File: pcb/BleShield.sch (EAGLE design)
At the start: 22 parts, among them U1 ARDUINO_SHIELDNOHOLES, Y1 32.768KHz, 10 PPM

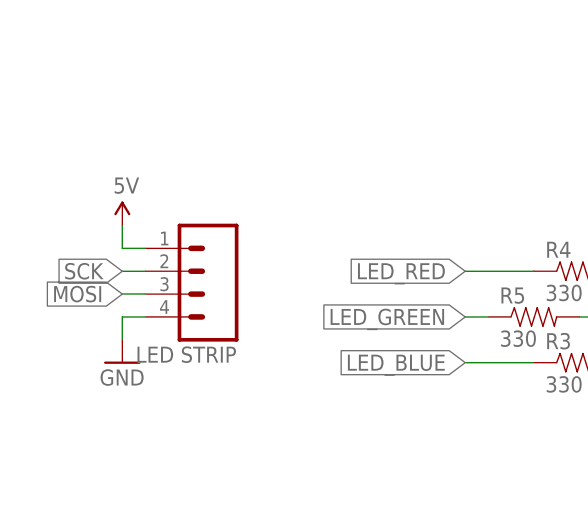
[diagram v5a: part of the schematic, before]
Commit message: fixed LED strip header, minor re-routing
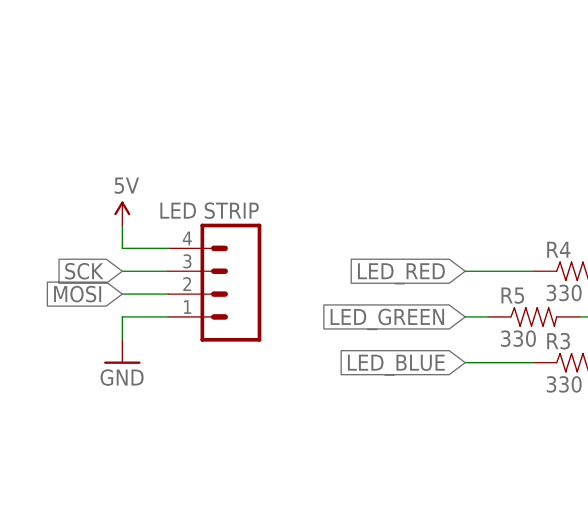
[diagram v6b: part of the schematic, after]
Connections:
- net 5V: now also LED STRIP.4; no longer LED STRIP.1
- net GND: now also LED STRIP.1; no longer LED STRIP.4
- net MOSI: now also LED STRIP.2; no longer LED STRIP.3
- net SCK: now also LED STRIP.3; no longer LED STRIP.2
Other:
- moved on the sheet: LED STRIP
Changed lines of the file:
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@@
 <instance part="GND6" gate="1" x="114.3" y="17.78"/>
 <instance part="R6" gate="G$1" x="104.14" y="83.82"/>
-<instance part="LED STRIP" gate="G$1" x="27.94" y="30.48" rot="R180"/>
+<instance part="LED STRIP" gate="G$1" x="30.48" y="27.94" rot="MR0"/>
 <instance part="GND7" gate="1" x="20.32" y="20.32"/>
 <instance part="U$2" gate="G$1" x="20.32" y="35.56"/>
@@
 </segment>
 <segment>
-<pinref part="LED STRIP" gate="G$1" pin="4"/>
-<wire x1="22.86" y1="25.4" x2="20.32" y2="25.4" width="0.1524" layer="91"/>
 <pinref part="GND7" gate="1" pin="GND"/>
 <wire x1="20.32" y1="25.4" x2="20.32" y2="22.86" width="0.1524" layer="91"/>
+<pinref part="LED STRIP" gate="G$1" pin="1"/>
+<wire x1="20.32" y1="25.4" x2="25.4" y2="25.4" width="0.1524" layer="91"/>
 </segment>
 <segment>
@@
 </segment>
 <segment>
-<pinref part="LED STRIP" gate="G$1" pin="3"/>
-<wire x1="22.86" y1="27.94" x2="20.32" y2="27.94" width="0.1524" layer="91"/>
+<pinref part="LED STRIP" gate="G$1" pin="2"/>
+<wire x1="25.4" y1="27.94" x2="20.32" y2="27.94" width="0.1524" layer="91"/>
 <label x="20.32" y="27.94" size="1.778" layer="95" rot="R180" xref="yes"/>
 </segment>
@@
 </segment>
 <segment>
-<pinref part="LED STRIP" gate="G$1" pin="2"/>
-<wire x1="22.86" y1="30.48" x2="20.32" y2="30.48" width="0.1524" layer="91"/>
+<pinref part="LED STRIP" gate="G$1" pin="3"/>
+<wire x1="25.4" y1="30.48" x2="20.32" y2="30.48" width="0.1524" layer="91"/>
 <label x="20.32" y="30.48" size="1.778" layer="95" rot="R180" xref="yes"/>
 </segment>
@@
 </segment>
 <segment>
-<pinref part="LED STRIP" gate="G$1" pin="1"/>
-<wire x1="22.86" y1="33.02" x2="20.32" y2="33.02" width="0.1524" layer="91"/>
 <pinref part="U$2" gate="G$1" pin="5V"/>
 <wire x1="20.32" y1="33.02" x2="20.32" y2="35.56" width="0.1524" layer="91"/>
-</segment>
-<segment>
+<pinref part="LED STRIP" gate="G$1" pin="4"/>
+<wire x1="20.32" y1="33.02" x2="25.4" y2="33.02" width="0.1524" layer="91"/>
+</segment>
+<segment>

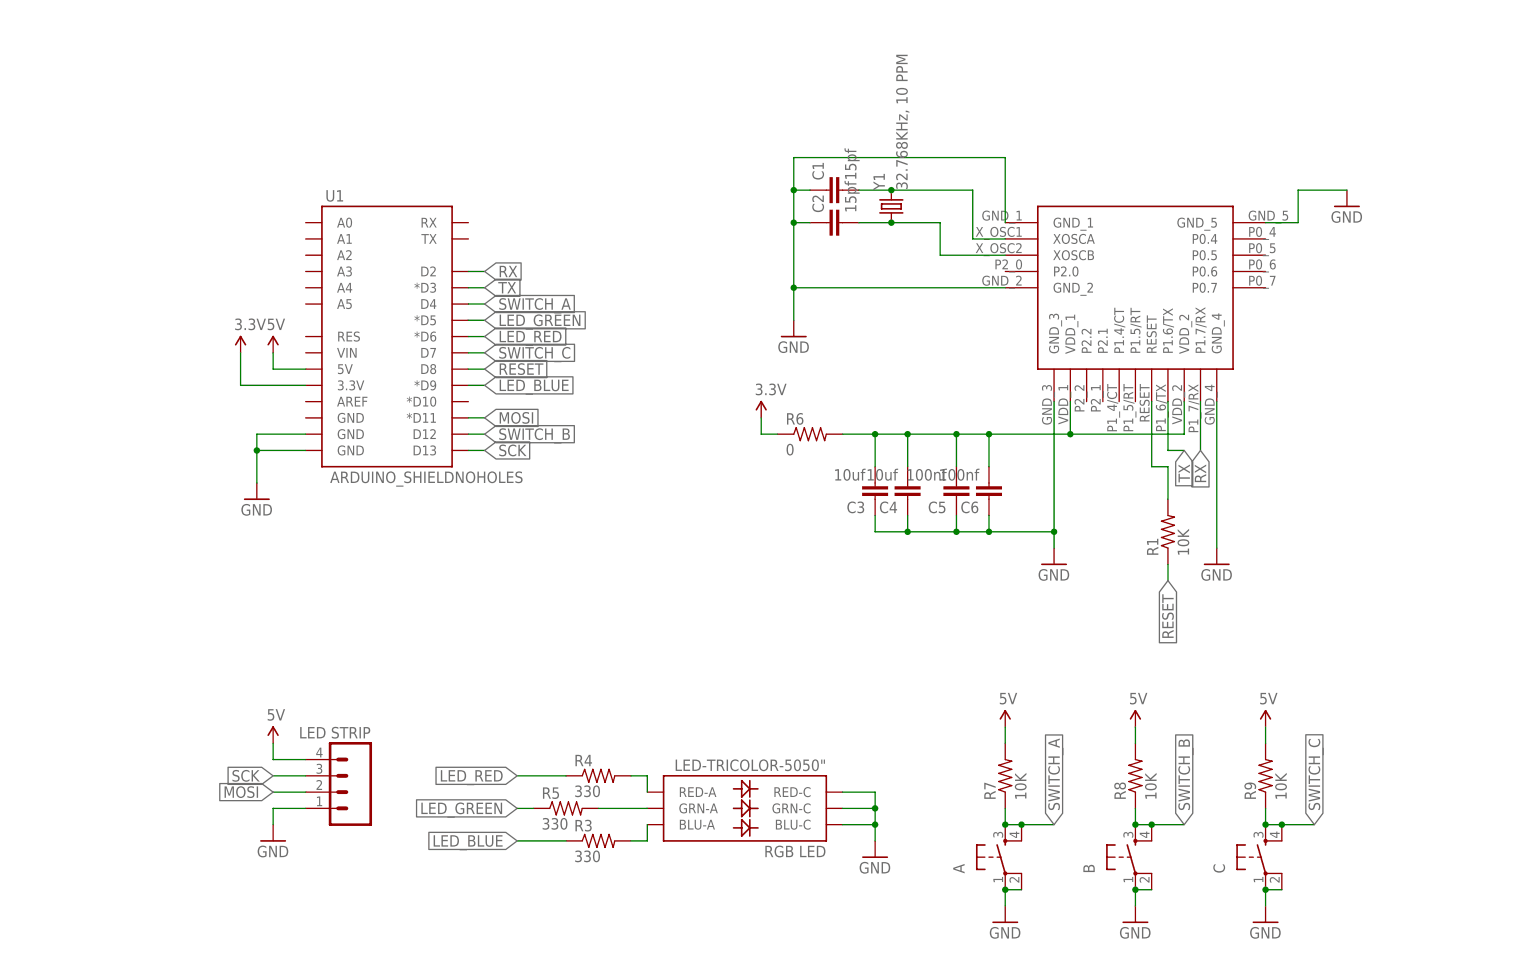
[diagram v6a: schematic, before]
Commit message: Update documentation, layout
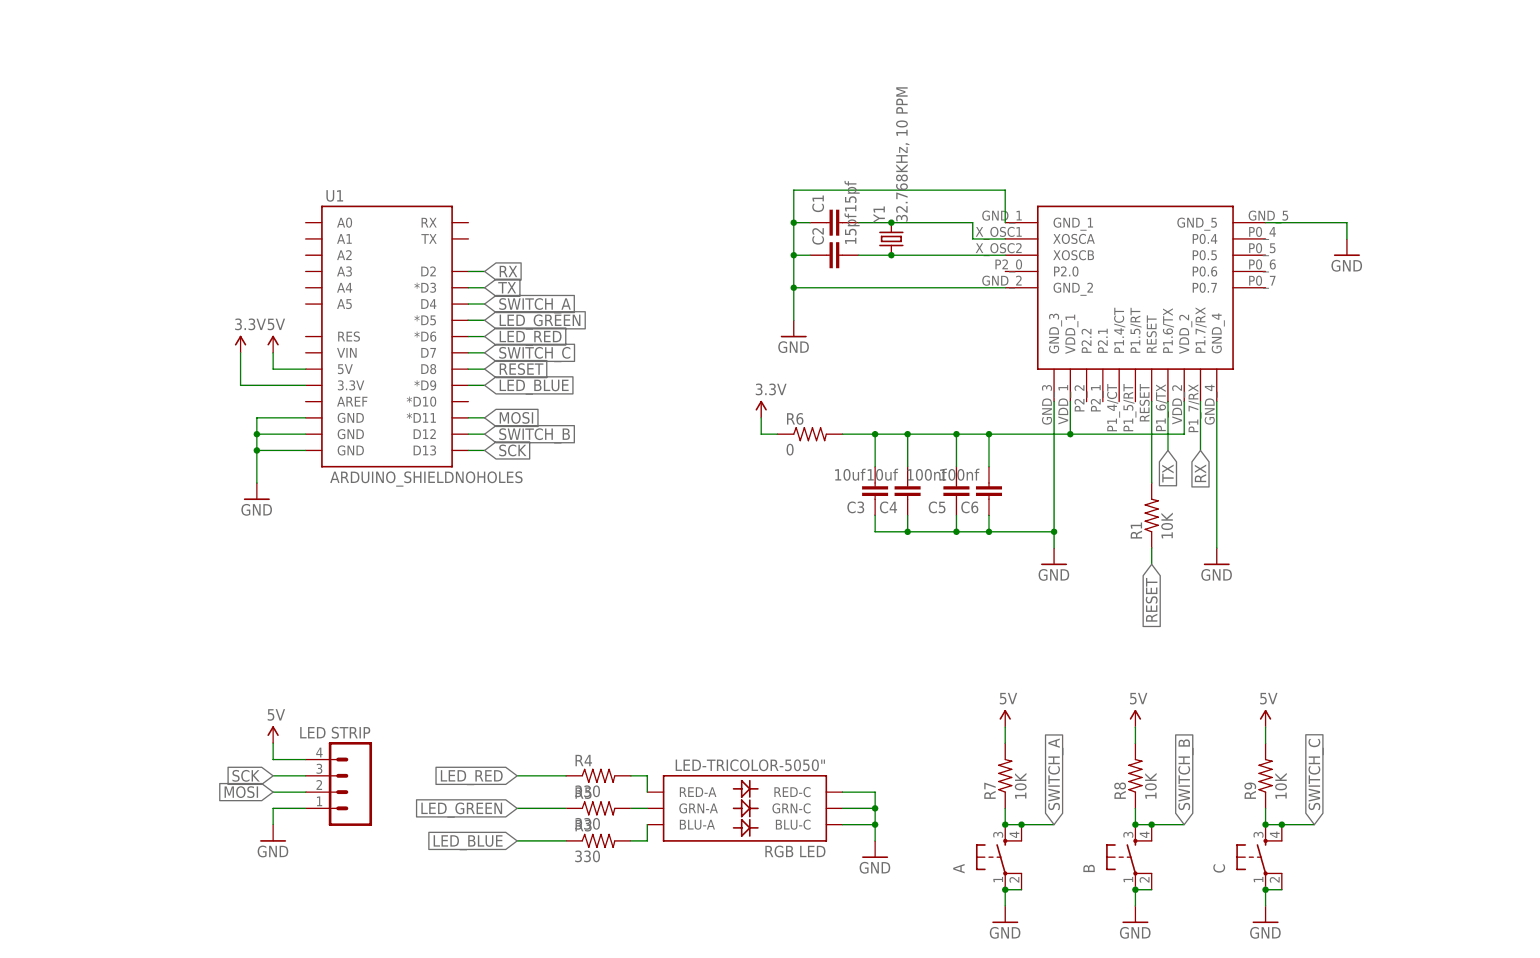
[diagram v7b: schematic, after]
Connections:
- net GND: now also U1.GND@2
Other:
- moved on the sheet: C1, C2, R1, R5, Y1
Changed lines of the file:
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@@
 <instance part="GND2" gate="1" x="142.24" y="63.5"/>
 <instance part="GND3" gate="1" x="101.6" y="99.06"/>
-<instance part="R1" gate="G$1" x="160.02" y="68.58" rot="R90"/>
-<instance part="GND4" gate="1" x="187.96" y="119.38"/>
+<instance part="R1" gate="G$1" x="157.48" y="71.12" rot="R90"/>
+<instance part="GND4" gate="1" x="187.96" y="111.76"/>
 <instance part="GND5" gate="1" x="167.64" y="63.5"/>
-<instance part="C1" gate="G$1" x="109.22" y="121.92" rot="R90"/>
-<instance part="C2" gate="G$1" x="109.22" y="116.84" rot="R90"/>
+<instance part="C1" gate="G$1" x="109.22" y="116.84" rot="R90"/>
+<instance part="C2" gate="G$1" x="109.22" y="111.76" rot="R90"/>
 <instance part="C3" gate="G$1" x="114.3" y="76.2" rot="R180"/>
 <instance part="C4" gate="G$1" x="119.38" y="76.2" rot="R180"/>
@@
 <instance part="R3" gate="G$1" x="71.12" y="20.32"/>
 <instance part="R4" gate="G$1" x="71.12" y="30.48"/>
-<instance part="R5" gate="G$1" x="66.04" y="25.4"/>
+<instance part="R5" gate="G$1" x="71.12" y="25.4"/>
 <instance part="GND6" gate="1" x="114.3" y="17.78"/>
 <instance part="R6" gate="G$1" x="104.14" y="83.82"/>
@@
 <instance part="GND10" gate="1" x="175.26" y="7.62"/>
 <instance part="RGB LED" gate="G$1" x="93.98" y="25.4" rot="R180"/>
-<instance part="Y1" gate="G$1" x="116.84" y="119.38" rot="R90"/>
+<instance part="Y1" gate="G$1" x="116.84" y="114.3" rot="R90"/>
 <instance part="A" gate="S" x="134.62" y="17.78" rot="R90"/>
 </instances>
@@
 <segment>
 <pinref part="U$1" gate="G$1" pin="P1.6/TX"/>
-<label x="162.56" y="81.28" size="1.778" layer="95" rot="R270" xref="yes"/>
-<wire x1="162.56" y1="81.28" x2="160.02" y2="81.28" width="0.1524" layer="91"/>
+<label x="160.02" y="81.28" size="1.778" layer="95" rot="R270" xref="yes"/>
 <wire x1="160.02" y1="81.28" x2="160.02" y2="88.9" width="0.1524" layer="91"/>
 </segment>
@@
 <wire x1="25.4" y1="81.28" x2="17.78" y2="81.28" width="0.1524" layer="91"/>
 <junction x="17.78" y="81.28"/>
+<pinref part="U1" gate="G$1" pin="GND@2"/>
+<wire x1="25.4" y1="86.36" x2="17.78" y2="86.36" width="0.1524" layer="91"/>
+<wire x1="17.78" y1="86.36" x2="17.78" y2="83.82" width="0.1524" layer="91"/>
+<junction x="17.78" y="83.82"/>
 </segment>
 <segment>
@@
 <wire x1="101.6" y1="106.68" x2="101.6" y2="101.6" width="0.1524" layer="91"/>
 <pinref part="U$1" gate="G$1" pin="GND_1"/>
-<wire x1="134.62" y1="116.84" x2="134.62" y2="127" width="0.1524" layer="91"/>
-<wire x1="134.62" y1="127" x2="101.6" y2="127" width="0.1524" layer="91"/>
-<wire x1="101.6" y1="127" x2="101.6" y2="121.92" width="0.1524" layer="91"/>
+<wire x1="134.62" y1="116.84" x2="134.62" y2="121.92" width="0.1524" layer="91"/>
+<wire x1="134.62" y1="121.92" x2="101.6" y2="121.92" width="0.1524" layer="91"/>
+<wire x1="101.6" y1="121.92" x2="101.6" y2="116.84" width="0.1524" layer="91"/>
 <junction x="101.6" y="106.68"/>
-<wire x1="101.6" y1="121.92" x2="101.6" y2="116.84" width="0.1524" layer="91"/>
-<wire x1="101.6" y1="116.84" x2="101.6" y2="106.68" width="0.1524" layer="91"/>
+<wire x1="101.6" y1="116.84" x2="101.6" y2="111.76" width="0.1524" layer="91"/>
+<wire x1="101.6" y1="111.76" x2="101.6" y2="106.68" width="0.1524" layer="91"/>
 <pinref part="C1" gate="G$1" pin="1"/>
-<wire x1="104.14" y1="121.92" x2="101.6" y2="121.92" width="0.1524" layer="91"/>
+<wire x1="104.14" y1="116.84" x2="101.6" y2="116.84" width="0.1524" layer="91"/>
 <pinref part="C2" gate="G$1" pin="1"/>
-<wire x1="104.14" y1="116.84" x2="101.6" y2="116.84" width="0.1524" layer="91"/>
-<junction x="101.6" y="121.92"/>
+<wire x1="104.14" y1="111.76" x2="101.6" y2="111.76" width="0.1524" layer="91"/>
 <junction x="101.6" y="116.84"/>
+<junction x="101.6" y="111.76"/>
 </segment>
 <segment>
@@
 <pinref part="U$1" gate="G$1" pin="GND_5"/>
 <pinref part="GND4" gate="1" pin="GND"/>
-<wire x1="175.26" y1="116.84" x2="180.34" y2="116.84" width="0.1524" layer="91"/>
-<wire x1="187.96" y1="121.92" x2="180.34" y2="121.92" width="0.1524" layer="91"/>
-<wire x1="180.34" y1="121.92" x2="180.34" y2="116.84" width="0.1524" layer="91"/>
+<wire x1="187.96" y1="114.3" x2="187.96" y2="116.84" width="0.1524" layer="91"/>
+<wire x1="187.96" y1="116.84" x2="175.26" y2="116.84" width="0.1524" layer="91"/>
 </segment>
 <segment>
@@
 <pinref part="U$1" gate="G$1" pin="RESET"/>
 <pinref part="R1" gate="G$1" pin="2"/>
-<wire x1="157.48" y1="88.9" x2="157.48" y2="78.74" width="0.1524" layer="91"/>
-<wire x1="157.48" y1="78.74" x2="160.02" y2="78.74" width="0.1524" layer="91"/>
-<wire x1="160.02" y1="78.74" x2="160.02" y2="73.66" width="0.1524" layer="91"/>
+<wire x1="157.48" y1="88.9" x2="157.48" y2="76.2" width="0.1524" layer="91"/>
 </segment>
 </net>
@@
 <segment>
 <pinref part="R1" gate="G$1" pin="1"/>
-<wire x1="160.02" y1="63.5" x2="160.02" y2="60.96" width="0.1524" layer="91"/>
-<label x="160.02" y="60.96" size="1.778" layer="95" rot="R270" xref="yes"/>
+<wire x1="157.48" y1="66.04" x2="157.48" y2="63.5" width="0.1524" layer="91"/>
+<label x="157.48" y="63.5" size="1.778" layer="95" rot="R270" xref="yes"/>
 </segment>
 <segment>
@@
 <segment>
 <pinref part="C1" gate="G$1" pin="2"/>
-<wire x1="111.76" y1="121.92" x2="116.84" y2="121.92" width="0.1524" layer="91"/>
-<wire x1="116.84" y1="121.92" x2="129.54" y2="121.92" width="0.1524" layer="91"/>
-<wire x1="129.54" y1="121.92" x2="129.54" y2="114.3" width="0.1524" layer="91"/>
+<wire x1="111.76" y1="116.84" x2="116.84" y2="116.84" width="0.1524" layer="91"/>
+<wire x1="116.84" y1="116.84" x2="129.54" y2="116.84" width="0.1524" layer="91"/>
+<wire x1="129.54" y1="116.84" x2="129.54" y2="114.3" width="0.1524" layer="91"/>
 <pinref part="U$1" gate="G$1" pin="XOSCA"/>
 <wire x1="129.54" y1="114.3" x2="134.62" y2="114.3" width="0.1524" layer="91"/>
 <pinref part="Y1" gate="G$1" pin="2"/>
-<junction x="116.84" y="121.92"/>
+<junction x="116.84" y="116.84"/>
 </segment>
 </net>
@@
 <segment>
 <pinref part="U$1" gate="G$1" pin="XOSCB"/>
-<wire x1="134.62" y1="111.76" x2="124.46" y2="111.76" width="0.1524" layer="91"/>
-<wire x1="124.46" y1="111.76" x2="124.46" y2="116.84" width="0.1524" layer="91"/>
-<wire x1="124.46" y1="116.84" x2="116.84" y2="116.84" width="0.1524" layer="91"/>
+<wire x1="134.62" y1="111.76" x2="116.84" y2="111.76" width="0.1524" layer="91"/>
 <pinref part="C2" gate="G$1" pin="2"/>
 <pinref part="Y1" gate="G$1" pin="1"/>
-<wire x1="116.84" y1="116.84" x2="111.76" y2="116.84" width="0.1524" layer="91"/>
-<junction x="116.84" y="116.84"/>
+<wire x1="116.84" y1="111.76" x2="111.76" y2="111.76" width="0.1524" layer="91"/>
+<junction x="116.84" y="111.76"/>
 </segment>
 </net>
@@
 <segment>
 <pinref part="R5" gate="G$1" pin="1"/>
-<wire x1="60.96" y1="25.4" x2="58.42" y2="25.4" width="0.1524" layer="91"/>
+<wire x1="66.04" y1="25.4" x2="58.42" y2="25.4" width="0.1524" layer="91"/>
 <label x="58.42" y="25.4" size="1.778" layer="95" rot="R180" xref="yes"/>
 </segment>
@@
 <pinref part="R5" gate="G$1" pin="2"/>
 <pinref part="RGB LED" gate="G$1" pin="GRN-A"/>
-<wire x1="71.12" y1="25.4" x2="78.74" y2="25.4" width="0.1524" layer="91"/>
-</segment>
-</net>
+<wire x1="76.2" y1="25.4" x2="78.74" y2="25.4" width="0.1524" layer="91"/>
+</segment>
+</net>

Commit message: Add keepaway, cutout to BLE part, knock out some to-do items.
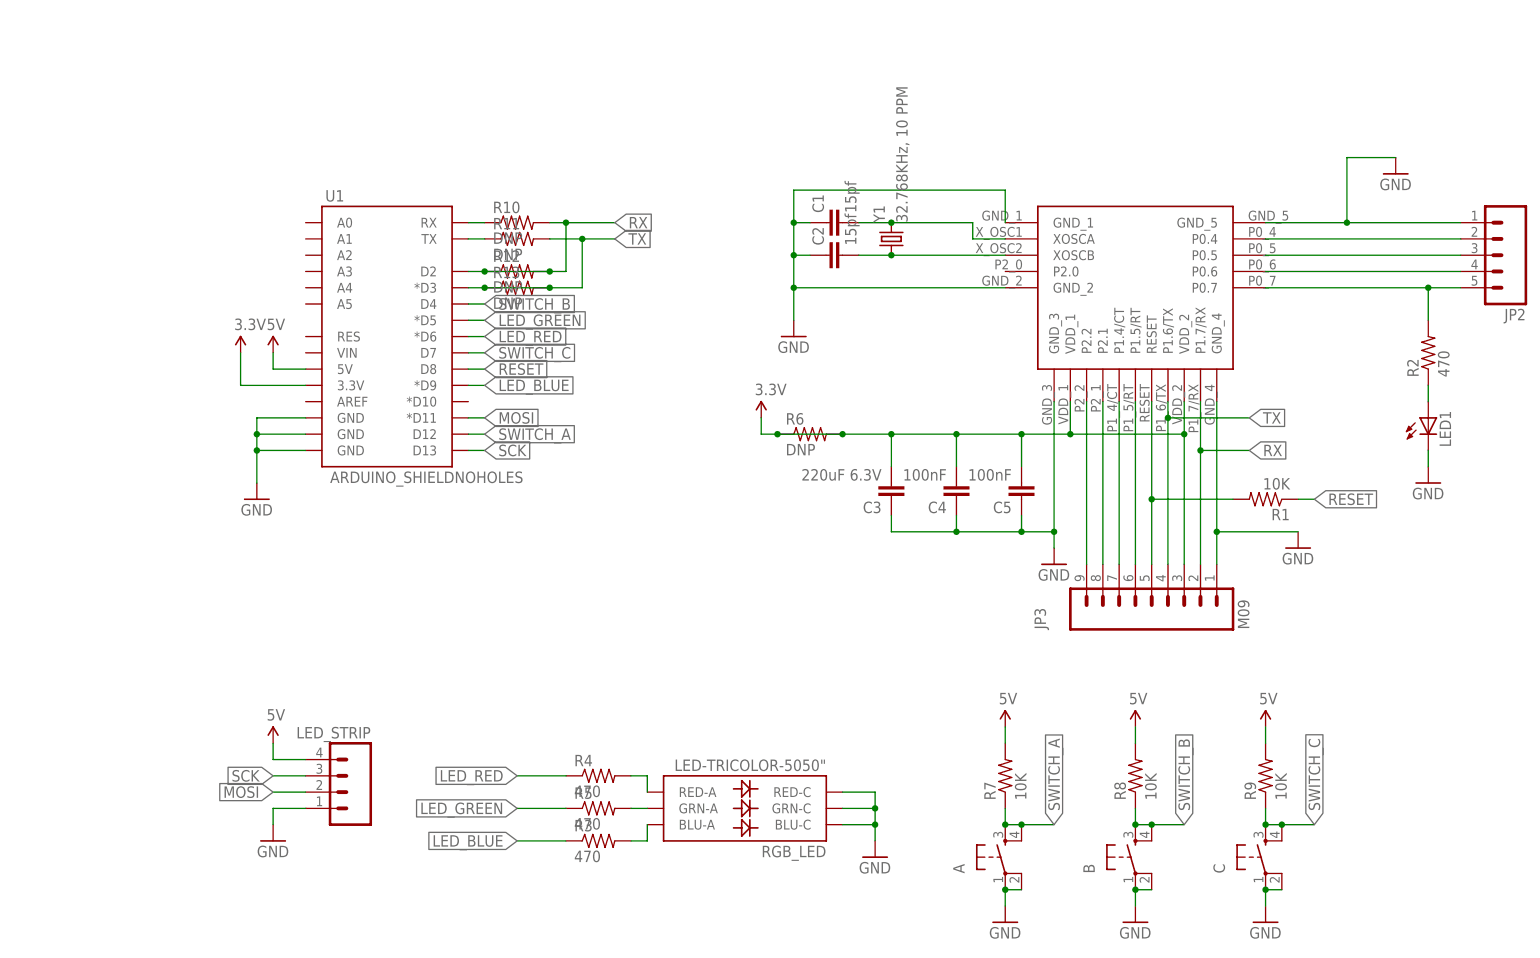
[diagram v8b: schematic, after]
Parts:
- LED_STRIP: renamed from LED STRIP
- RGB_LED: renamed from RGB LED
- removed C6: 100nf, SparkFun:CAP0805
- added JP2: (no value), SparkFun:M05PTH
- added JP3: M09, SparkFun:M09
- added LED1: (no value), adafruit:LEDCHIPLED_0805
- added R10, R11, R12, R13: DNP, SparkFun:RESISTOR0805-RES
- added R2: 470, SparkFun:RESISTOR0805-RES
- C3: value 10uf -> 220uF 6.3V
- C4: value 10uf -> 100nF
- C5: value 100nf -> 100nF
- R3, R4, R5: value 330 -> 470
- R6: value 0 -> DNP
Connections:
- new net N$10: R10.1, U1.RX
- new net N$11: R11.1, U1.TX
- new net N$12: JP3.8, U$1.P2.1
- new net N$13: JP3.7, U$1.P1.4/CT
- new net N$14: JP3.6, U$1.P1.5/RT
- new net N$15: JP2.2, U$1.P0.4
- new net N$16: JP2.3, U$1.P0.5
- new net N$18: JP2.4, U$1.P0.6
- new net N$7: LED1.A, R2.1
- new net N$9: JP2.5, R2.2, U$1.P0.7
- net 3.3V: now also C3.2, C4.2, C5.2, JP3.3, R6.2, U$1.VDD_1, U$1.VDD_2
- net GND: now also JP2.1, JP3.1, LED1.C; no longer C6.1
- net N$1: now also JP3.5
- net N$8: now also JP3.9, U$1.P2.2; no longer C3.2, C4.2, C5.2, C6.2, R6.2, U$1.VDD_1, U$1.VDD_2
- net RX: now also JP3.2, R10.2, R12.1, R12.2
- net SWITCH_A: now also U1.D12; no longer U1.D4
- net SWITCH_B: now also U1.D4; no longer U1.D12
- net TX: now also JP3.4, R11.2, R13.1, R13.2
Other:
- moved on the sheet: C3, C4, C5, R1
